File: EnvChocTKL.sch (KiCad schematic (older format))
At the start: 181 parts, among them U1 EliteC

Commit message: added mount holes, a few silkscreen marks and generated revision 0 gerber
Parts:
- added H1, H2, H3, H4: MountingHole_Pad, MountingHole:MountingHole_2.5mm_Pad, symbol Mechanical:MountingHole_Pad
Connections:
- net GND: now also H1.1, H2.1, H3.1, H4.1
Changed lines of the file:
@@
 	1    0    0    -1
 $EndComp
+$Comp
+L Mechanical:MountingHole_Pad H1
+U 1 1 613EF488
+P 10100 7450
+F 0 "H1" H 10200 7453 50  0000 L CNN
+F 1 "MountingHole_Pad" H 10200 7408 50  0001 L CNN
+F 2 "MountingHole:MountingHole_2.5mm_Pad" H 10100 7450 50  0001 C CNN
+F 3 "~" H 10100 7450 50  0001 C CNN
+	1    10100 7450
+	1    0    0    -1
+$EndComp
+$Comp
+L Mechanical:MountingHole_Pad H2
+U 1 1 613F0F2A
+P 10400 7450
+F 0 "H2" H 10500 7453 50  0000 L CNN
+F 1 "MountingHole_Pad" H 10500 7408 50  0001 L CNN
+F 2 "MountingHole:MountingHole_2.5mm_Pad" H 10400 7450 50  0001 C CNN
+F 3 "~" H 10400 7450 50  0001 C CNN
+	1    10400 7450
+	1    0    0    -1
+$EndComp
+$Comp
+L Mechanical:MountingHole_Pad H3
+U 1 1 613F142B
+P 10700 7450
+F 0 "H3" H 10800 7453 50  0000 L CNN
+F 1 "MountingHole_Pad" H 10800 7408 50  0001 L CNN
+F 2 "MountingHole:MountingHole_2.5mm_Pad" H 10700 7450 50  0001 C CNN
+F 3 "~" H 10700 7450 50  0001 C CNN
+	1    10700 7450
+	1    0    0    -1
+$EndComp
+$Comp
+L Mechanical:MountingHole_Pad H4
+U 1 1 613F17DC
+P 11000 7450
+F 0 "H4" H 11100 7453 50  0000 L CNN
+F 1 "MountingHole_Pad" H 11100 7408 50  0001 L CNN
+F 2 "MountingHole:MountingHole_2.5mm_Pad" H 11000 7450 50  0001 C CNN
+F 3 "~" H 11000 7450 50  0001 C CNN
+	1    11000 7450
+	1    0    0    -1
+$EndComp
+Wire Wire Line
+	10100 7550 10100 7650
+Wire Wire Line
+	11000 7550 11000 7650
+Connection ~ 11000 7650
+Wire Wire Line
+	11000 7650 11050 7650
+Wire Wire Line
+	10700 7550 10700 7650
+Connection ~ 10700 7650
+Wire Wire Line
+	10700 7650 11000 7650
+Wire Wire Line
+	10400 7550 10400 7650
+Wire Wire Line
+	10100 7650 10400 7650
+Connection ~ 10400 7650
+Wire Wire Line
+	10400 7650 10700 7650
+$Comp
+L power:GND #PWR01
+U 1 1 614A57C4
+P 11050 7650
+F 0 "#PWR01" H 11050 7400 50  0001 C CNN
+F 1 "GND" V 11055 7522 50  0000 R CNN
+F 2 "" H 11050 7650 50  0001 C CNN
+F 3 "" H 11050 7650 50  0001 C CNN
+	1    11050 7650
+	0    -1   -1   0
+$EndComp
 $EndSCHEMATC

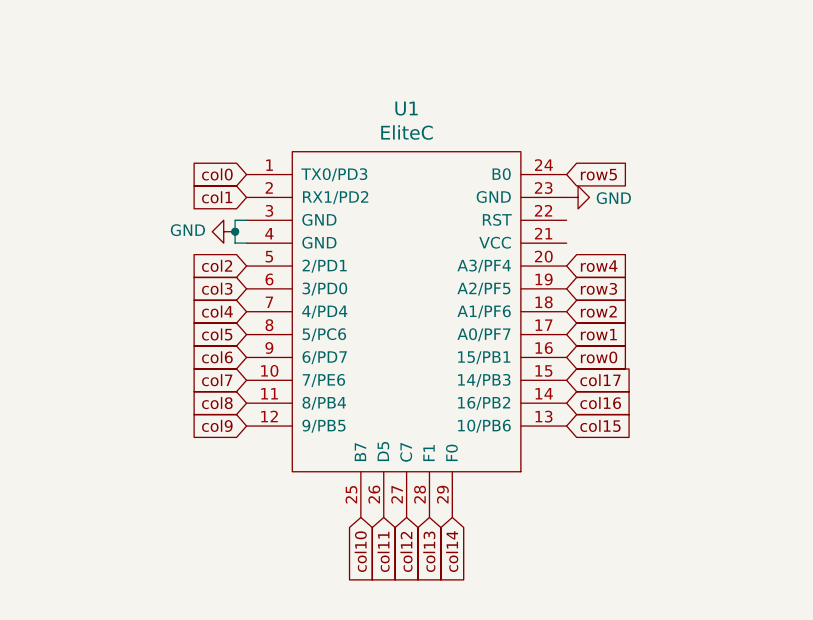
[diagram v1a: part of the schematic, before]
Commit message: moved MCU and redid a bunch of traces
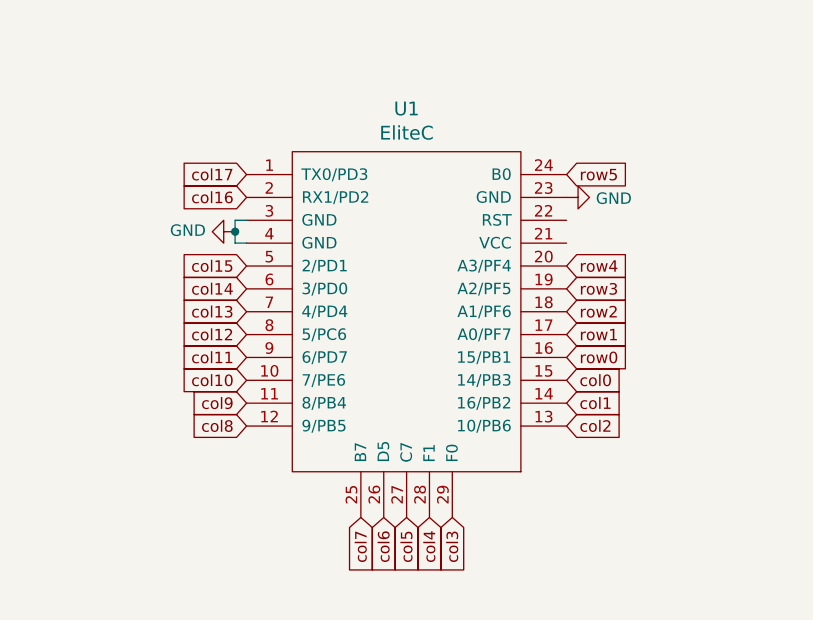
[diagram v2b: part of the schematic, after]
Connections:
- net col0: now also U1.15 (14/PB3); no longer U1.1 (TX0/PD3)
- net col1: now also U1.14 (16/PB2); no longer U1.2 (RX1/PD2)
- net col10: now also U1.10 (7/PE6); no longer U1.25 (B7)
- net col11: now also U1.9 (6/PD7); no longer U1.26 (D5)
- net col12: now also U1.8 (5/PC6); no longer U1.27 (C7)
- net col13: now also U1.7 (4/PD4); no longer U1.28 (F1)
- net col14: now also U1.6 (3/PD0); no longer U1.29 (F0)
- net col15: now also U1.5 (2/PD1); no longer U1.13 (10/PB6)
- net col16: now also U1.2 (RX1/PD2); no longer U1.14 (16/PB2)
- net col17: now also U1.1 (TX0/PD3); no longer U1.15 (14/PB3)
- net col2: now also U1.13 (10/PB6); no longer U1.5 (2/PD1)
- net col3: now also U1.29 (F0); no longer U1.6 (3/PD0)
- net col4: now also U1.28 (F1); no longer U1.7 (4/PD4)
- net col5: now also U1.27 (C7); no longer U1.8 (5/PC6)
- net col6: now also U1.26 (D5); no longer U1.9 (6/PD7)
- net col7: now also U1.25 (B7); no longer U1.10 (7/PE6)
- net col8: now also U1.12 (9/PB5); no longer U1.11 (8/PB4)
- net col9: now also U1.11 (8/PB4); no longer U1.12 (9/PB5)
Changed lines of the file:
@@
 	1    0    0    -1
 $EndComp
-Text GLabel 5950 8650 2    50   Input ~ 0
-col15
-Text GLabel 5950 8550 2    50   Input ~ 0
-col16
-Text GLabel 5950 8450 2    50   Input ~ 0
-col17
 Text GLabel 5950 8350 2    50   Input ~ 0
 row0
@@
 Text GLabel 5950 7550 2    50   Input ~ 0
 row5
-Text GLabel 5450 9050 3    50   Input ~ 0
-col14
-Text GLabel 5350 9050 3    50   Input ~ 0
-col13
-Text GLabel 5250 9050 3    50   Input ~ 0
-col12
-Text GLabel 5150 9050 3    50   Input ~ 0
-col11
-Text GLabel 5050 9050 3    50   Input ~ 0
-col10
-Text GLabel 4550 8650 0    50   Input ~ 0
-col9
-Text GLabel 4550 8550 0    50   Input ~ 0
-col8
-Text GLabel 4550 8450 0    50   Input ~ 0
-col7
-Text GLabel 4550 8350 0    50   Input ~ 0
-col6
-Text GLabel 4550 8250 0    50   Input ~ 0
-col5
-Text GLabel 4550 8150 0    50   Input ~ 0
-col4
-Text GLabel 4550 8050 0    50   Input ~ 0
-col3
-Text GLabel 4550 7950 0    50   Input ~ 0
-col2
-Text GLabel 4550 7550 0    50   Input ~ 0
-col0
-Text GLabel 4550 7650 0    50   Input ~ 0
-col1
 $Comp
 L power:GND #PWR0101
@@
 Wire Wire Line
 	4500 7750 4550 7750
-Wire Wire Line
-	4500 7800 4500 7850
-Wire Wire Line
-	4500 7800 4500 7750
-Connection ~ 4500 7800
-$Comp
-L power:GND #PWR0102
-U 1 1 613F350E
-P 4500 7800
-F 0 "#PWR0102" H 4500 7550 50  0001 C CNN
-F 1 "GND" V 4505 7672 50  0000 R CNN
-F 2 "" H 4500 7800 50  0001 C CNN
-F 3 "" H 4500 7800 50  0001 C CNN
-	1    4500 7800
-	0    1    -1   0
-$EndComp
-$Comp
-L keebio:Elite-C U1
-U 1 1 613EDFBC
-P 5250 8100
-F 0 "U1" H 5250 8937 60  0000 C CNN
-F 1 "EliteC" H 5250 8831 60  0000 C CNN
-F 2 "Keebio-Parts:Elite-C" V 6300 5600 60  0001 C CNN
-F 3 "" V 6300 5600 60  0001 C CNN
-	1    5250 8100
-	1    0    0    -1
-$EndComp
 $Comp
 L Mechanical:MountingHole_Pad H1
@@
 	0    -1   -1   0
 $EndComp
+Connection ~ 4500 7800
+Wire Wire Line
+	4500 7800 4500 7750
+Wire Wire Line
+	4500 7800 4500 7850
+$Comp
+L power:GND #PWR0102
+U 1 1 613F350E
+P 4500 7800
+F 0 "#PWR0102" H 4500 7550 50  0001 C CNN
+F 1 "GND" V 4505 7672 50  0000 R CNN
+F 2 "" H 4500 7800 50  0001 C CNN
+F 3 "" H 4500 7800 50  0001 C CNN
+	1    4500 7800
+	0    1    -1   0
+$EndComp
+Text GLabel 5450 9050 3    50   Input ~ 0
+col3
+Text GLabel 5350 9050 3    50   Input ~ 0
+col4
+Text GLabel 5250 9050 3    50   Input ~ 0
+col5
+Text GLabel 5150 9050 3    50   Input ~ 0
+col6
+Text GLabel 5050 9050 3    50   Input ~ 0
+col7
+Text GLabel 4550 8650 0    50   Input ~ 0
+col8
+Text GLabel 4550 8550 0    50   Input ~ 0
+col9
+Text GLabel 4550 8450 0    50   Input ~ 0
+col10
+Text GLabel 4550 8350 0    50   Input ~ 0
+col11
+Text GLabel 4550 8250 0    50   Input ~ 0
+col12
+Text GLabel 4550 8150 0    50   Input ~ 0
+col13
+Text GLabel 4550 8050 0    50   Input ~ 0
+col14
+Text GLabel 4550 7550 0    50   Input ~ 0
+col17
+Text GLabel 4550 7650 0    50   Input ~ 0
+col16
+Text GLabel 4550 7950 0    50   Input ~ 0
+col15
+Text GLabel 5950 8650 2    50   Input ~ 0
+col2
+Text GLabel 5950 8450 2    50   Input ~ 0
+col0
+Text GLabel 5950 8550 2    50   Input ~ 0
+col1
+$Comp
+L keebio:Elite-C U1
+U 1 1 613EDFBC
+P 5250 8100
+F 0 "U1" H 5250 8937 60  0000 C CNN
+F 1 "EliteC" H 5250 8831 60  0000 C CNN
+F 2 "Keebio-Parts:Elite-C" V 6300 5600 60  0001 C CNN
+F 3 "" V 6300 5600 60  0001 C CNN
+	1    5250 8100
+	1    0    0    -1
+$EndComp
 $EndSCHEMATC

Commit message: fixed issues with footprint and required board changes + updated gerber
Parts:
- K_0, K_1, K_10, K_11, K_12, K_13, K_14, K_15, K_16, K_17, K_18, K_19, K_2, K_20, K_21, K_22, K_23, K_24, K_25, K_26, K_27, K_28, K_3, K_30, K_31, K_32, K_34, K_35, K_36, K_37, K_38, K_39, K_4, K_40, K_41, K_42, K_43, K_44, K_45, K_47, K_48, K_49, K_5, K_51, K_52, K_53, K_54, K_55, K_56, K_57, K_58, K_59, K_6, K_60, K_61, K_62, K_64, K_65, K_66, K_67, K_68, K_69, K_7, K_70, K_71, K_72, K_73, K_74, K_76, K_8, K_85, K_86, K_87, K_9: footprint Switch_Keyboard_Kailh:SW_Kailh_Choc_V1_1.00u -> Switch_Keyboard_Kailh:SW_Kailh_Choc_V2
- K_29: footprint Switch_Keyboard_Kailh:SW_Kailh_Choc_V1_2.00u -> Switch_Keyboard_Kailh:SW_Kailh_Choc_V2
- K_33: footprint Switch_Keyboard_Kailh:SW_Kailh_Choc_V1_1.50u -> Switch_Keyboard_Kailh:SW_Kailh_Choc_V2
- K_46: footprint Switch_Keyboard_Kailh:SW_Kailh_Choc_V1_ISOEnter -> Switch_Keyboard_Kailh:SW_Kailh_Choc_V2
- K_50: footprint Switch_Keyboard_Kailh:SW_Kailh_Choc_V1_1.75u -> Switch_Keyboard_Kailh:SW_Kailh_Choc_V2
- K_63, K_77, K_78, K_79, K_81, K_82, K_83, K_84: footprint Switch_Keyboard_Kailh:SW_Kailh_Choc_V1_1.25u -> Switch_Keyboard_Kailh:SW_Kailh_Choc_V2
- K_75: footprint Switch_Keyboard_Kailh:SW_Kailh_Choc_V1_2.75u -> Switch_Keyboard_Kailh:SW_Kailh_Choc_V2
- K_80: footprint Switch_Keyboard_Kailh:SW_Kailh_Choc_V1_6.25u -> Switch_Keyboard_Kailh:SW_Kailh_Choc_V2
